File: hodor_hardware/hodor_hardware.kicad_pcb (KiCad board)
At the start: 2 copper layers, 153.6 x 86 mm, 275 parts, among them J1 Screw_Terminal_01x02, J10 Screw_Terminal_01x02, J12 Conn_01x24_Pin, J13 Conn_01x24_Socket, J14 Screw_Terminal_01x02, J15 Screw_Terminal_01x02, J16 Screw_Terminal_01x02, J17 Screw_Terminal_01x02, J3 Screw_Terminal_01x03, J4 USB_C_Receptacle_USB2.0_16P, J5 Screw_Terminal_01x03, J6 Screw_Terminal_01x04, J7 Screw_Terminal_01x02, J8 Screw_Terminal_01x02, J9 Conn_01x04_Pin, K1 FINDER-32.21-x000, K2 FINDER-32.21-x000, Q1 SiS443DN, Q10 BC847BDW1, Q2 FDG1024NZ, Q3 FDG1024NZ, Q4 IRLML9301, Q5 BSS138, Q6 BSS138DW, Q7 SiS443DN, Q8 2V7002, Q9 IRLML9301, SW1 SW_RST, SW2 SW_BOOT, T1 GND, T10 V_{BUS}, T11 3V3, T12 5V, T14 V_{BUS}_SENSE, T15 I_SNS, T16 D_FB, T17 D_PWM2, T18 D_PWM1, T19 VC_OUT, T20 V_LDSNS, T21 SCL, T22 VC_CMP, T23 VC_REF, T24 SDA, T25 DRV_EN, T26 DRV_SF, T27 SF_Q, T28 SF_TRG, T29 SF_CLR, T30 ENC_B, T31 ENC_A, T32 GND, T4 IN2, T5 IN1, T6 V_{DC}_SENSE, T7 IN3, T8 IN4, T9 V_{DC}, U1 ESP32-S3-WROOM-1_N8R2, U10 LM4040DBZ-2.5, U11 MCP6561x-LT, U12 MC33HB2002, U13 74LVC1G123, U14 ACS722xLCTR-10AB, U15 TPS2116DRL, U16 MCP23S08-xML, U17 SSD1306, U2 TLV62569DBV, U3 74LVC2G14, U4 74LVC2G14, U5 TPS54240DRC, U6 MAX811SEUS-T, U7 74LVC2G14, U8 ZXTR2105F, U9 24LC256

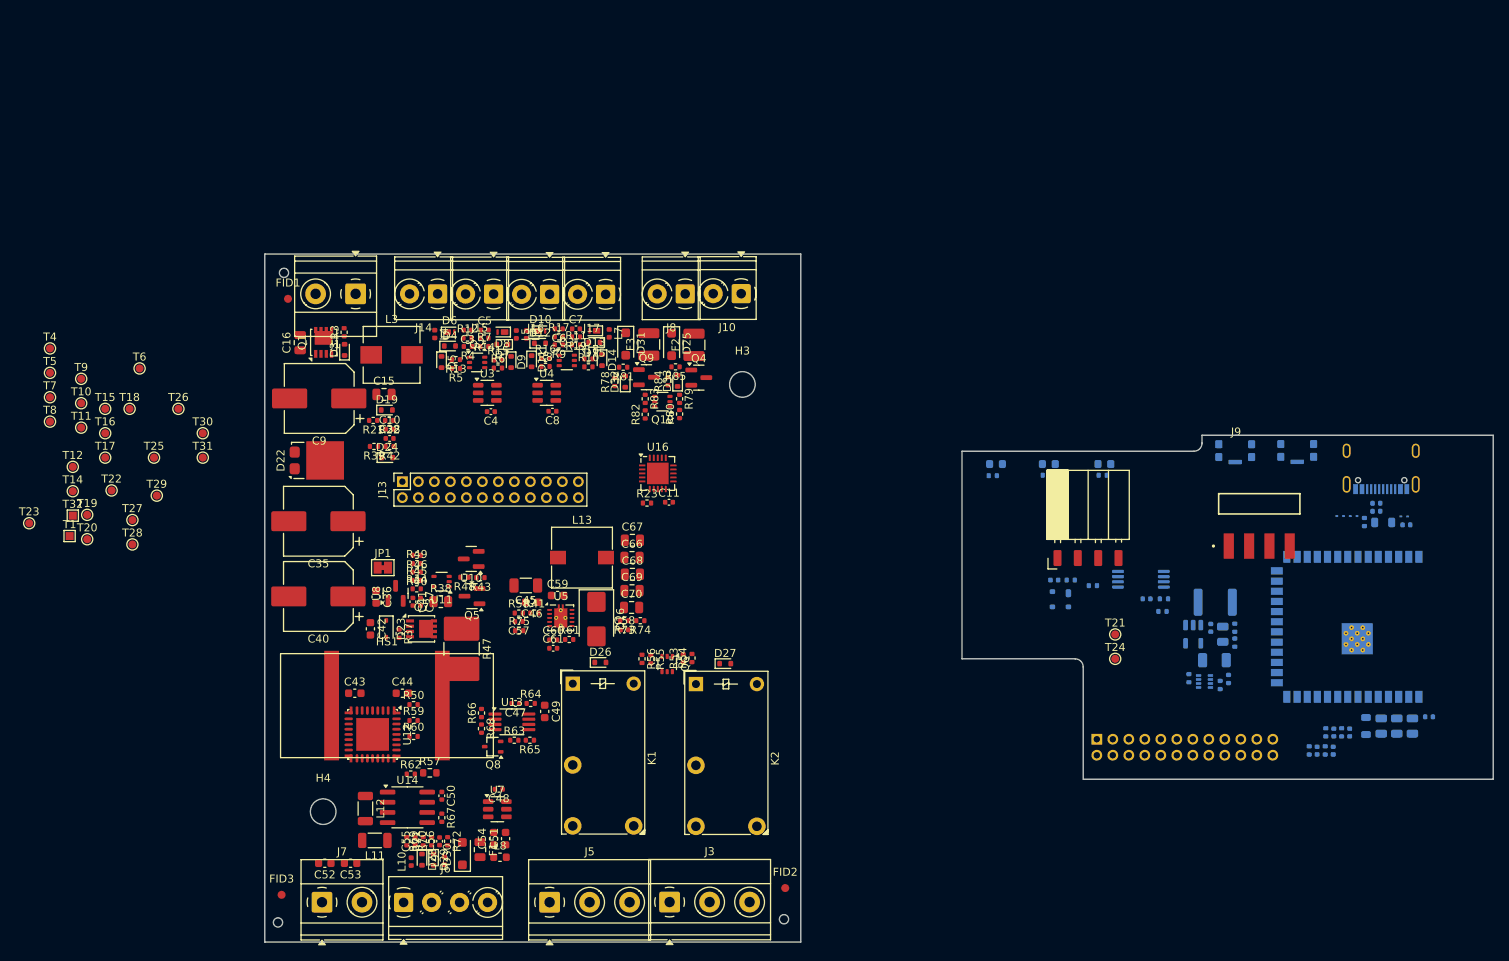
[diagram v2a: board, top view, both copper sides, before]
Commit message: Finished schematic and initial placement on PCB
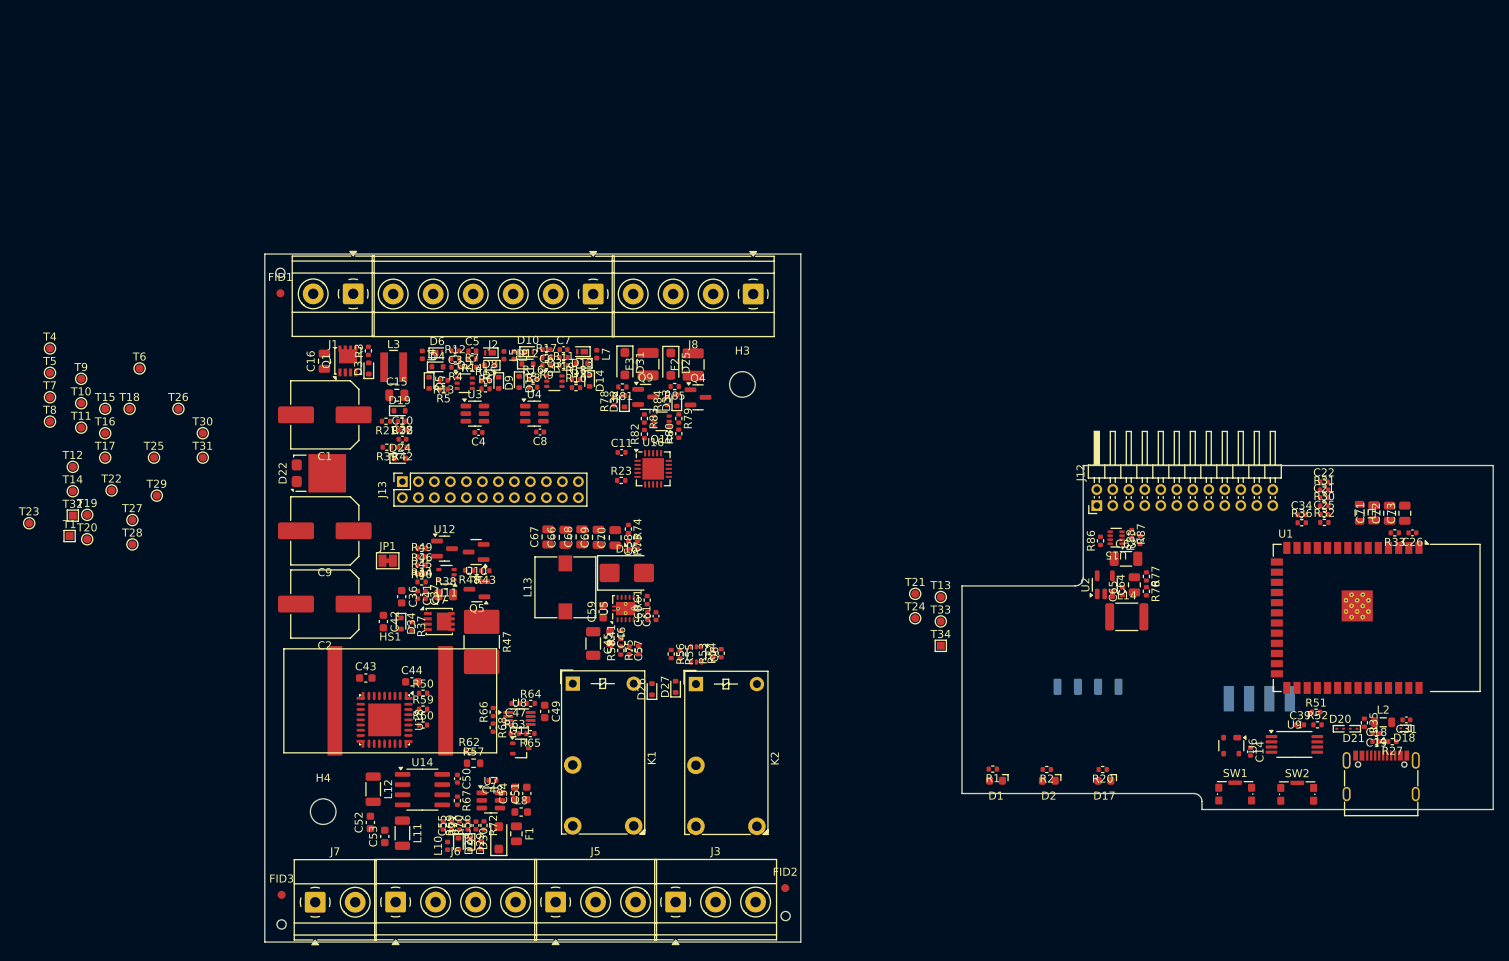
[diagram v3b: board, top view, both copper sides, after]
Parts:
- removed C35, C40: 100u/50V, Capacitor_SMD:CP_Elec_8x10.5
- removed D23: BZX384-C15V, Diode_SMD:D_SOD-323
- removed H1, H2, H5: JLCPCB_ToolingHole, mm_parts_footprints:JLCPCB_ToolingHole
- removed J10, J14, J15, J16, J17: Screw_Terminal_01x02, TerminalBlock_Phoenix:TerminalBlock_Phoenix_PT-1,5-2-3.5-H_1x02_P3.50mm_Horizontal
- removed Q8: 2V7002, Package_TO_SOT_SMD:SOT-323_SC-70
- removed U13: 74LVC1G123, Package_SO:MSOP-8_3x3mm_P0.65mm
- added C1: 100uF/50V, Capacitor_SMD:C_Elec_8x10.2, F.Cu at (55.3, 67.3)
- added C2: 100uF/50V, Capacitor_SMD:C_Elec_8x10.2, F.Cu at (55.3, 91.0)
- added D34: BCX84C15V, Diode_SMD:D_SOD-523, F.Cu at (64.8, 93.4)
- added H6: JLCPCB_ToolingHole, hodor_footprints:JLCPCB_ToolingHole, F.Cu at (49.9, 131.0)
- added H7: JLCPCB_ToolingHole, hodor_footprints:JLCPCB_ToolingHole, F.Cu at (49.8, 49.5)
- added H8: JLCPCB_ToolingHole, hodor_footprints:JLCPCB_ToolingHole, F.Cu at (112.9, 129.9)
- added J2: Screw_Terminal_01x06, TerminalBlock_Phoenix:TerminalBlock_Phoenix_MKDS-1,5-6_1x06_P5.00mm_Horizontal, F.Cu at (88.8, 52.2)
- added Q11: 2V7002, Package_TO_SOT_SMD:SOT-323_SC-70, F.Cu at (79.8, 109.0)
- added T13: 5V, TestPoint:TestPoint_Pad_D1.0mm, F.Cu at (132.3, 90.1)
- added T33: 3V3, TestPoint:TestPoint_Pad_D1.0mm, F.Cu at (132.3, 93.1)
- added T34: GND, TestPoint:TestPoint_Pad_1.0x1.0mm, F.Cu at (132.3, 96.2)
- added U18: MC33HB2002, hodor_footprints:HVQFN-28-1EP_6x6mm_MC33HB2002, F.Cu at (62.8, 105.4)
- C14, C18, C19, C26, C31, C39, C63, C64, C65, C71, C72, C73, D1, D17, D18, D2, D20, D21, J12, J4, L1, L14, L2, R1, R2, R20, R27, R30, R31, R32, R33, R35, R36, R51, R52, R76, R77, R86, R87, R88, SW1, SW2, U1, U15, U2, U6, U9: moved to F.Cu
- C21, C22, C25, C34: value 100p -> 1n; moved to F.Cu
- C9: value 100u/50V -> 100uF/50V; footprint Capacitor_SMD:CP_Elec_8x10.5 -> Capacitor_SMD:C_Elec_8x10.2
- J6: footprint TerminalBlock_Phoenix:TerminalBlock_Phoenix_PT-1,5-4-3.5-H_1x04_P3.50mm_Horizontal -> TerminalBlock_Phoenix:TerminalBlock_Phoenix_MKDS-1,5-4_1x04_P5.00mm_Horizontal
- J8: value Screw_Terminal_01x02 -> Screw_Terminal_01x04; footprint TerminalBlock_Phoenix:TerminalBlock_Phoenix_PT-1,5-2-3.5-H_1x02_P3.50mm_Horizontal -> TerminalBlock_Phoenix:TerminalBlock_Phoenix_MKDS-1,5-4_1x04_P5.00mm_Horizontal
- J9, U17: moved to B.Cu
- L3: value 4.7uH/3.5A -> 4.7uH/4A; footprint Inductor_SMD:L_Wuerth_HCI-7030 -> Inductor_SMD:L_Wuerth_MAPI-4020
- Q2, Q3: value FDG1024NZ -> BSS138DW
- R22, R42: value 2.2k -> 2k
- U12: value MC33HB2002 -> ZXTR2105F; footprint mm_parts_footprints:HVQFN-28-1EP_6x6mm_MC33HB2002 -> Package_TO_SOT_SMD:SOT-23
- U8: value ZXTR2105F -> 74LVC1G123; footprint Package_TO_SOT_SMD:SOT-23 -> Package_SO:VSSOP-8_2.3x2mm_P0.5mm
- moved SW2 43.0 mm to (176.8, 114.7)
- moved SW1 42.9 mm to (169.1, 114.7)
- moved R27 42.2 mm to (188.7, 108.2)
- moved R33 40.9 mm to (189.1, 82.0)
- moved J4 40.8 mm to (187.3, 113.6)
- moved D1 39.6 mm to (139.2, 113.0)
- moved D17 39.6 mm to (152.8, 113.0)
- moved D2 39.6 mm to (145.8, 113.0)
- moved R2 36.8 mm to (145.6, 111.6)
- moved R20 36.8 mm to (152.5, 111.6)
- moved R1 36.7 mm to (138.8, 111.6)
- moved C14 32.6 mm to (171.0, 109.4), turned to -90 degrees
- moved C22 31.5 mm to (180.2, 75.7), turned to 0 degrees
- moved R31 30.4 mm to (180.2, 76.7), turned to 0 degrees
- moved C18 29.8 mm to (186.8, 108.1)
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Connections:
- C15 pad 1: V_{DC} -> VDC
- C36 pad 1: V_{BUS} -> VBUS
- C42 pad 1: V_{BUS} -> VBUS
- C43 pad 1: V_{BUS} -> VBUS
- C43 pad 2: Net-(U12-CCP) -> Net-(U18-CCP)
- C45 pad 1: V_{DC} -> VDC
- C46 pad 1: V_{DC} -> VDC
- C49 pad 1: Net-(U13A-RCext) -> Net-(U8A-RCext)
- C49 pad 2: Net-(U13A-Cext) -> Net-(U8A-Cext)
- C9 pad 1: V_{DC} -> VBUS
- D22 pad 1: V_{DC} -> VDC
- D22 pad 2: V_{DC} -> VDC
- D22 pad 3: V_{BUS} -> VBUS
- D32 pad 1: V_{DC} -> VDC
- D33 pad 1: V_{DC} -> VDC
- J12 pad 1: Net-(J12-Pin_1) -> 5V_BOARD
- J12 pad 10: /Controllerboard/SPI_~{CS1} -> /Controllerboard/SPI_~{CS0}
- J12 pad 11: /Controllerboard/SPI_~{CS0} -> /Controllerboard/SPI_SCK
- J12 pad 13: /Controllerboard/SPI_SCK -> /Controllerboard/SPI_MOSI
- J12 pad 14: /Controllerboard/SPI_MOSI -> /Controllerboard/ENC_A
- J12 pad 15: GNDD -> /Controllerboard/ENC_B
- J12 pad 16: /Controllerboard/ENC_A -> /Controllerboard/IO_MUX_INT
- J12 pad 17: /Controllerboard/ENC_B -> /Controllerboard/IO_MUX_~{RST}
- J12 pad 18: GNDD -> /Controllerboard/D_PWM1
- J12 pad 19: /Controllerboard/D_PWM1 -> /Controllerboard/D_PWM2
- J12 pad 2: Net-(J12-Pin_2) -> GNDD
- J12 pad 20: /Controllerboard/D_PWM2 -> GNDD
- J12 pad 21: 5V_BOARD -> Net-(J12-Pin_21)
- J12 pad 22: GNDD -> Net-(J12-Pin_22)
- J12 pad 23: VD3V3 -> Net-(J12-Pin_23)
- J12 pad 24: GNDD -> Net-(J12-Pin_24)
- J12 pad 3: Net-(J12-Pin_3) -> VD3V3
- J12 pad 4: Net-(J12-Pin_4) -> GNDD
- J12 pad 5: GNDD -> /Controllerboard/SF_~{CLR}
- J12 pad 6: /Controllerboard/SF_~{CLR} -> /Controllerboard/SF_TRG
- J12 pad 7: /Controllerboard/SF_TRG -> /Controllerboard/D_EN
- J12 pad 8: /Controllerboard/D_EN -> /Controllerboard/D_~{SF}
- J12 pad 9: /Controllerboard/D_~{SF} -> /Controllerboard/SPI_~{CS1}
- J13 pad 1: /Controllerboard/ADC_CH1 -> +5V
- J13 pad 10: /Controllerboard/~{CS1} -> /Controllerboard/~{CS0}
- J13 pad 11: /Controllerboard/~{CS0} -> /Controllerboard/SCK
- J13 pad 12: /Controllerboard/SCK -> /Controllerboard/MISO
- J13 pad 13: /Controllerboard/MISO -> /Controllerboard/MOSI
- J13 pad 14: /Controllerboard/MISO -> /Controllerboard/ENCODER_A
- J13 pad 15: GND -> /Controllerboard/ENCODER_B
- J13 pad 16: /Controllerboard/ENCODER_A -> /Controllerboard/IO_INT
- J13 pad 17: /Controllerboard/ENCODER_B -> /Controllerboard/IO_~{RST}
- J13 pad 18: GND -> /Controllerboard/DRV_PWM1
- J13 pad 19: /Controllerboard/DRV_PWM1 -> /Controllerboard/DRV_PWM2
- J13 pad 2: /Controllerboard/ADC_CH2 -> GND
- J13 pad 20: /Controllerboard/DRV_PWM2 -> GND
- J13 pad 21: +5V -> /Controllerboard/ADC_CH1
- J13 pad 22: GND -> /Controllerboard/ADC_CH2
- J13 pad 23: +3V3 -> /Controllerboard/ADC_CH3
- J13 pad 24: GND -> /Controllerboard/ADC_CH4
- J13 pad 3: /Controllerboard/ADC_CH3 -> +3V3
- J13 pad 4: /Controllerboard/ADC_CH4 -> GND
- J13 pad 5: GND -> /Controllerboard/SAFETY_~{CLR}
- J13 pad 6: /Controllerboard/SAFETY_~{CLR} -> /Controllerboard/SAFETY_TRIG
- J13 pad 7: /Controllerboard/SAFETY_TRIG -> /Controllerboard/DRV_EN
- J13 pad 8: /Controllerboard/DRV_EN -> /Controllerboard/DRV_~{SF}
- J13 pad 9: /Controllerboard/DRV_~{SF} -> /Controllerboard/~{CS1}
- J8 pad 1: Net-(D31-K) -> Net-(D25-K)
- JP1 pad 1: V_{BUS} -> VBUS
- L3 pad 2: V_{DC} -> VDC
- Q4 pad 2: V_{DC} -> VDC
- Q7 pad 1: V_{BUS} -> VBUS
- Q7 pad 2: V_{BUS} -> VBUS
- Q7 pad 3: V_{BUS} -> VBUS
- Q9 pad 2: V_{DC} -> VDC
- R21 pad 2: V_{DC} -> VDC
- R23 pad 2: /Peripherals/IO_~{RST} -> /Controllerboard/IO_~{RST}
- R30 pad 1: Net-(J12-Pin_2) -> Net-(J12-Pin_22)
- R31 pad 1: Net-(J12-Pin_1) -> Net-(J12-Pin_21)
- R32 pad 1: Net-(J12-Pin_3) -> Net-(J12-Pin_23)
- R36 pad 1: Net-(J12-Pin_4) -> Net-(J12-Pin_24)
- R37 pad 1: V_{BUS} -> VBUS
- R39 pad 2: V_{BUS} -> VBUS
- R41 pad 2: V_{DC} -> VDC
- R64 pad 2: Net-(U13A-RCext) -> Net-(U8A-RCext)
- R65 pad 1: Net-(U13A-Q) -> Net-(U8A-Q)
- R78 pad 1: V_{DC} -> VDC
- R84 pad 1: V_{DC} -> VDC
- T10 pad 1: V_{BUS} -> VBUS
- T27 pad 1: Net-(U13A-Q) -> Net-(U8A-Q)
- T9 pad 1: V_{DC} -> VDC
- U1 pad 22: unconnected-(U1-IO14-Pad22) -> /Controllerboard/LED_CONN
- U1 pad 32: unconnected-(U1-IO39-Pad32) -> /Controllerboard/IO_MUX_INT
- U1 pad 33: unconnected-(U1-IO40-Pad33) -> /Controllerboard/IO_MUX_~{RST}
- U1 pad 8: unconnected-(U1-IO15-Pad8) -> /Controllerboard/LED_ACTIVE
- U1 pad 9: unconnected-(U1-IO16-Pad9) -> /Controllerboard/LED_STATUS
- U12 pad 1: /Controllerboard/MISO -> GND
- U12 pad 2: /Controllerboard/SCK -> Net-(U11-V+)
- U12 pad 3: /Controllerboard/MOSI -> VBUS
- U16 pad 1: /Peripherals/MISO -> /Controllerboard/MISO
- U16 pad 19: /Peripherals/SCK -> /Controllerboard/SCK
- U16 pad 20: /Peripherals/MOSI -> /Controllerboard/MOSI
- U16 pad 4: /Peripherals/IO_~{RST} -> /Controllerboard/IO_~{RST}
- U16 pad 5: /Peripherals/~{CS1} -> /Controllerboard/~{CS1}
- U16 pad 7: /Peripherals/IO_INT -> /Controllerboard/IO_INT
- U5 pad 2: V_{DC} -> VDC
- U8 pad 2: Net-(U11-V+) -> /Controllerboard/SAFETY_TRIG
- U8 pad 3: V_{BUS} -> /Controllerboard/SAFETY_~{CLR}
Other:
- outline, holes or cut-outs redrawn

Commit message: Initialized SW project
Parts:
- D10, D13, D6, D8: footprint Diode_SMD:Nexperia_DSN1608-2_1.6x0.8mm -> Diode_SMD:D_SOD-523
- moved C67 12.1 mm to (83.2, 94.7), turned to 180 degrees
- moved R75 12.0 mm to (97.2, 85.0), turned to 180 degrees
- moved R74 11.5 mm to (82.2, 84.6), turned to 0 degrees
- moved C57 11.3 mm to (97.3, 86.2), turned to 0 degrees
- moved R58 10.7 mm to (97.3, 87.2), turned to 180 degrees
- moved C61 10.3 mm to (93.0, 82.8), turned to 180 degrees
- moved C58 10.3 mm to (84.2, 83.5), turned to 180 degrees
- moved C66 10.1 mm to (83.2, 92.5), turned to 180 degrees
- moved R56 9.97 mm to (108.4, 95.4), turned to 90 degrees
- moved C45 9.18 mm to (96.4, 90.7), turned to 0 degrees
- moved R73 9.15 mm to (84.2, 84.6), turned to 0 degrees
- moved C70 9.09 mm to (83.2, 86.2), turned to 180 degrees
- moved C60 8.96 mm to (93.0, 83.9), turned to 180 degrees
- moved C68 8.94 mm to (83.2, 90.4), turned to 180 degrees
- moved C69 8.52 mm to (83.2, 88.3), turned to 180 degrees
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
